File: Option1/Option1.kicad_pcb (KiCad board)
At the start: 2 copper layers, 86 x 69.5 mm, 115 parts, among them J1501 GH-13AB, J1801 Conn_01x08_Socket, J401 Conn_01x05_Pin, J402 Conn_01x04_Pin, J403 Conn_01x05_Pin, J503 KF2EDGKRG-3.5-2*7P, Q1001 JY2302, Q1101 JY2302, Q1401 BC817-40, Q1402 BC817-40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

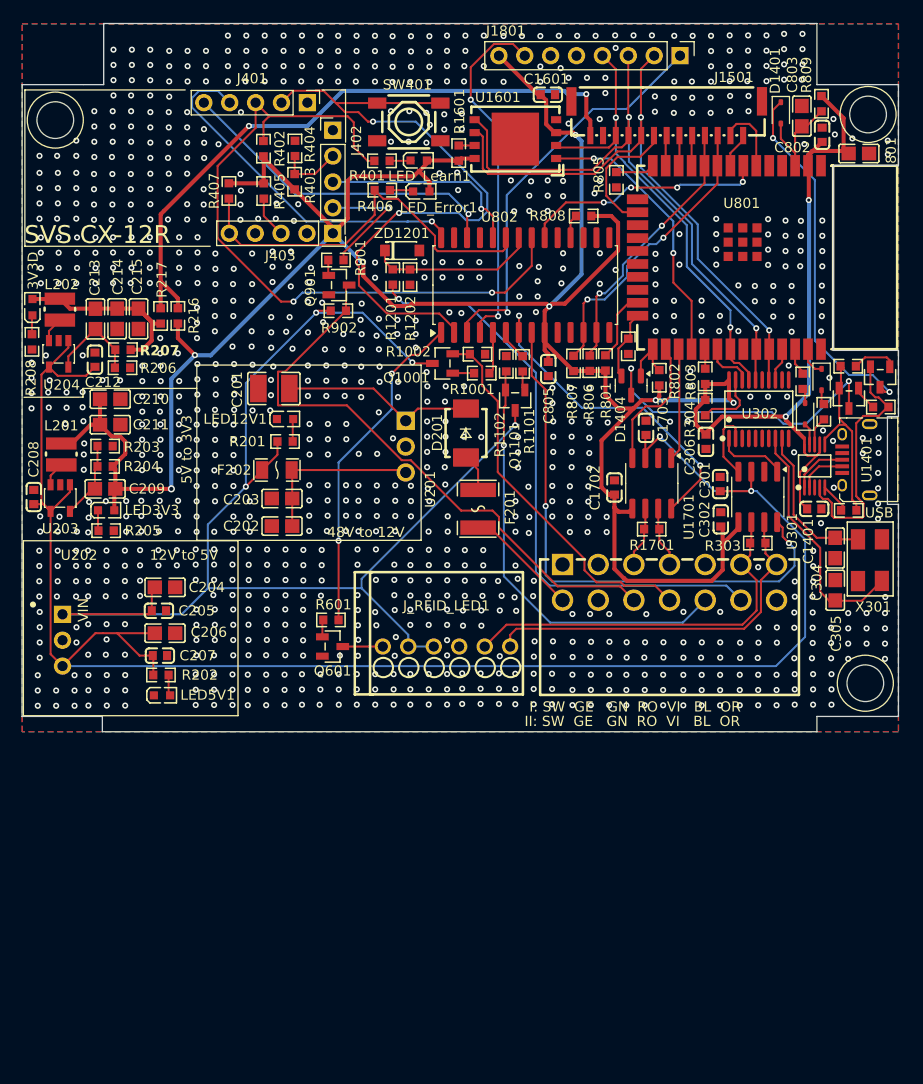
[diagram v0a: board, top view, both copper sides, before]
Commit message: Stecker nach hinten verschoben, Platine am vorderen Rand verlängert, Farbprints + Ref Feld hinzugefügt, Review eingearbeitet: Leiterbahnen dicker gemacht für Spannungsversorgung, Löcher verschoben, KeepOut Area vergrößert
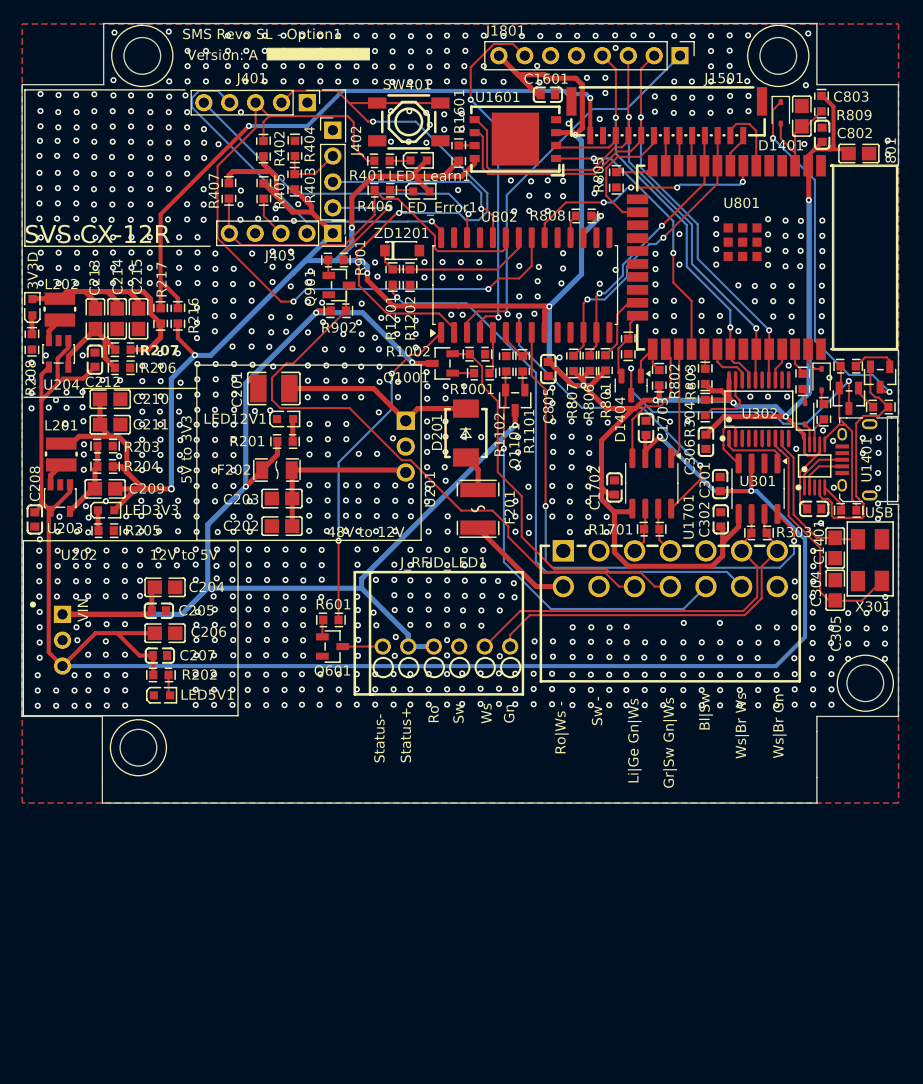
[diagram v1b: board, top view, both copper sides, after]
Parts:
- moved C208 2.20 mm to (101.2, 92.6), turned to -90 degrees
- moved J503 1.34 mm to (163.6, 97.5)
- moved R303 1.00 mm to (172.3, 94.0)
- moved U301 0.81 mm to (172.2, 89.6)
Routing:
- net 3.3V: track 310.7 -> 338.5 mm, vias 9 -> 12
- net /Powersupply/3.3V_D1: track 19.8 -> 27.3 mm
- net 5V: track 173.2 -> 177.2 mm
- net Lernmodus: track 67.5 -> 65.4 mm
- net /CAN2_Tranciever/CAN_S-Mode: track 54.7 -> 52.7 mm
- net /CAN1 Tranciever/CAN_H: track 6.51 -> 4.64 mm
- net Net-(U204-FB): track 9.45 -> 11.1 mm
- net /CAN1 Tranciever/CAN_L: track 5.95 -> 4.58 mm
- net /SOC Schalter/SOC_VCU: track 42.8 -> 41.5 mm
- net /RemoteDrive Schalter/RemoteDrive_VCU: track 36.9 -> 38.1 mm
- net /Stecker Input/VCU_LED: track 58.9 -> 57.8 mm
- net /CAN2_Tranciever/CAN_RX: track 7.00 -> 6.26 mm
- net GND: vias 1017 -> 991
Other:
- board size 86 x 69.5 mm -> 86 x 76.5 mm
- board text added: "Bl|Sw"
- board text added: "Gn"
- board text added: "Gr|Sw Gn|Ws"
- board text added: "Li|Ge Gn|Ws"
- board text added: "Ro"
- board text added: "Ro|Ws -"
- board text added: "SMS Revo SL - Option1"
- board text added: "Status+"
- board text added: "Status-"
- board text added: "Sw"
- board text added: "Sw -"
- board text added: "Version: A"
- board text added: "Ws"
- board text added: "Ws|Br Gn"
- board text added: "Ws|Br Ws"
- board text removed: "I: SW GE GN RO VI BL OR"
- board text removed: "II: SW GE GN RO VI BL OR"
- board text removed: "SMS Revo SL - Option1 - V1.0"

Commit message: Minimale Änderungen, Ausschnitt für USB Größer
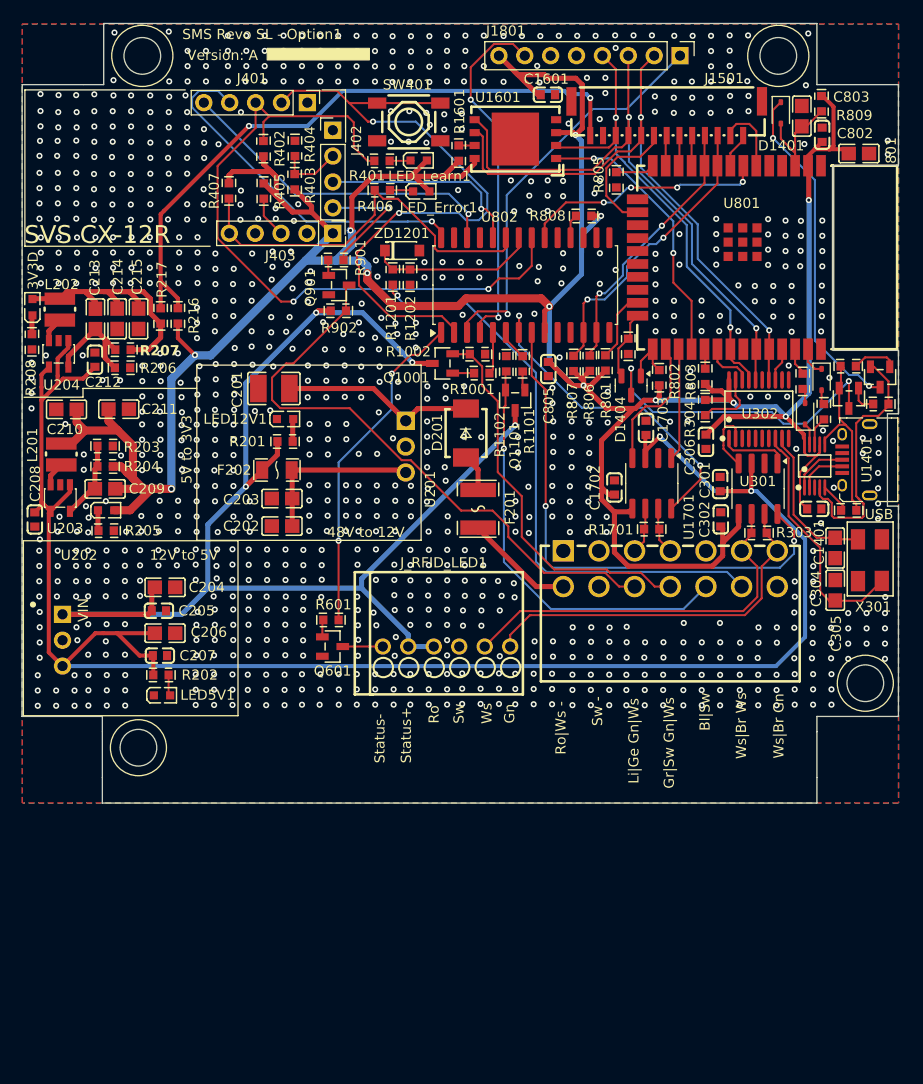
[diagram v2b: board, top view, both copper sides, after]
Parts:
- moved C210 4.41 mm to (104.3, 81.8), turned to 180 degrees
- moved C211 1.74 mm to (109.4, 81.8)
- moved R1404 0.30 mm to (184.2, 81.3)
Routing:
- net Net-(D1401-K): track 35.9 -> 33.8 mm
- net 3.3V: track 338.5 -> 339.8 mm
- net GND: vias 991 -> 973
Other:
- outline, holes or cut-outs redrawn

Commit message: LEDs für RX Ausgänge des Funkmodules hinzugefügt
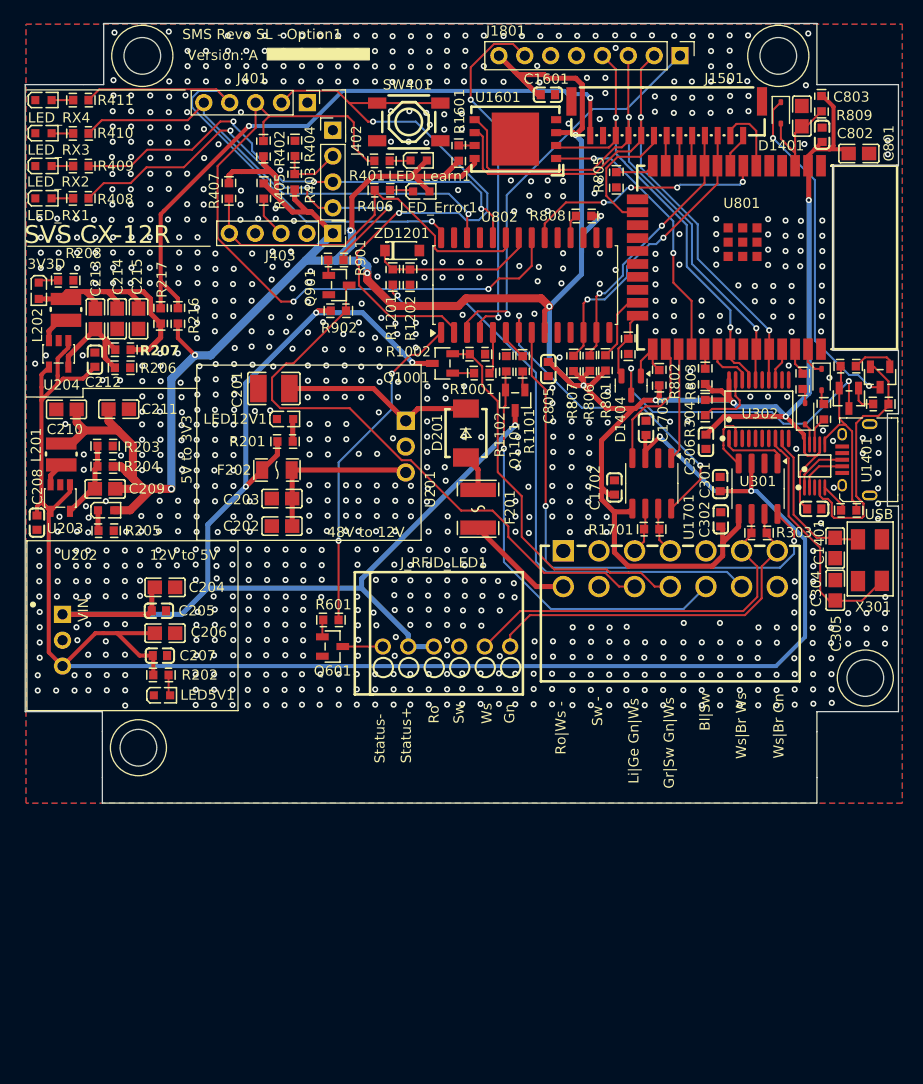
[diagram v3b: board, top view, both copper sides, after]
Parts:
- added LED_RX1: XL-1608SYGC-06, easyeda2kicad:LED0603-RD_GREEN, F.Cu at (102.0, 61.1)
- added LED_RX2: XL-1608SYGC-06, easyeda2kicad:LED0603-RD_GREEN, F.Cu at (102.0, 58.0)
- added LED_RX3: XL-1608SYGC-06, easyeda2kicad:LED0603-RD_GREEN, F.Cu at (102.0, 54.7)
- added LED_RX4: XL-1608SYGC-06, easyeda2kicad:LED0603-RD_GREEN, F.Cu at (102.0, 51.5)
- added R408: 220Ω, easyeda2kicad:R0603, F.Cu at (105.7, 61.1)
- added R409: 220Ω, easyeda2kicad:R0603, F.Cu at (105.7, 58.0)
- added R410: 220Ω, easyeda2kicad:R0603, F.Cu at (105.7, 54.8)
- added R411: 220Ω, easyeda2kicad:R0603, F.Cu at (105.7, 51.5)
- moved R208 6.89 mm to (104.2, 69.2), turned to 0 degrees
- moved 3V3D 1.72 mm to (101.6, 70.2), turned to -90 degrees
- moved L202 0.60 mm to (104.2, 72.0)
- moved C208 0.37 mm to (101.4, 93.0)
- renumbered 801 to C801
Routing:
- net RX_1: track 12.3 -> 42.9 mm, vias 1 -> 3
- net RX_2: track 19.9 -> 48.8 mm, vias 1 -> 3
- net RX_4: track 35.3 -> 50.2 mm
- net RX_3: track 32.7 -> 46.0 mm
- net Net-(LED_RX3-A): track 0.00 -> 2.13 mm
- net Net-(LED_RX4-A): track 0.00 -> 2.12 mm
- net Net-(LED_RX2-A): track 0.00 -> 2.12 mm
- net Net-(LED_RX1-A): track 0.00 -> 2.12 mm
- net /Powersupply/3.3V_D1: track 27.3 -> 26.7 mm
- net GND: vias 973 -> 925
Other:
- board size 86 x 76.5 mm -> 85.7 x 76.5 mm

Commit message: Kabelseitigen Stecker für JLC Bestellung hinzugefügt. Footprint erstellt und 3D Modell hinzugefügt, Footprint/3DModell von 6Pin Stecker und Fuse korrigiert
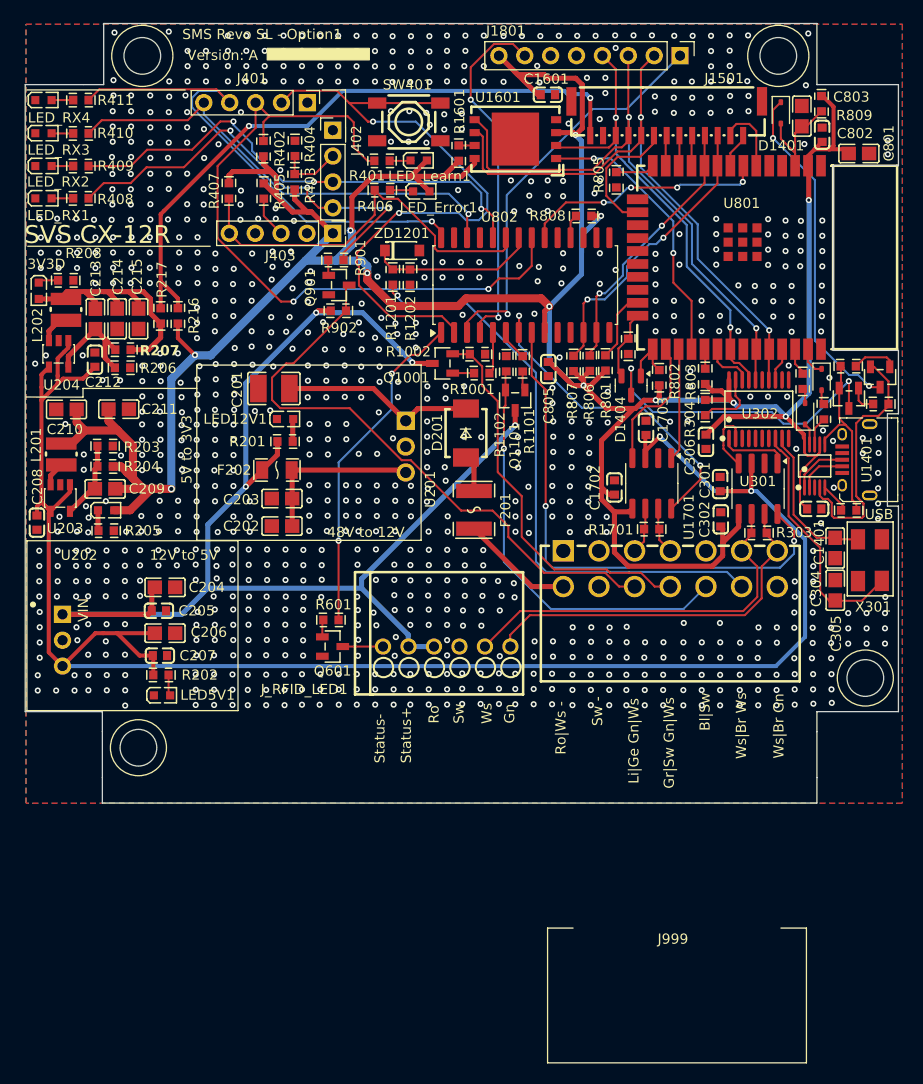
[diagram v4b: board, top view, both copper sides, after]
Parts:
- added J999: Phoenix_Connetor_07x2pin_toWire, easyeda2kicad:Phonix_Connector_07x2pin_toWire, F.Cu at (151.5, 146.0)
- moved J_RFID_LED1 10.1 mm to (132.6, 109.8)
- moved F201 3.31 mm to (146.3, 94.5)

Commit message: Platine verkleinert, um besser in gehäuse zu passen, PullUp Widerstand an Button hinzugefügt
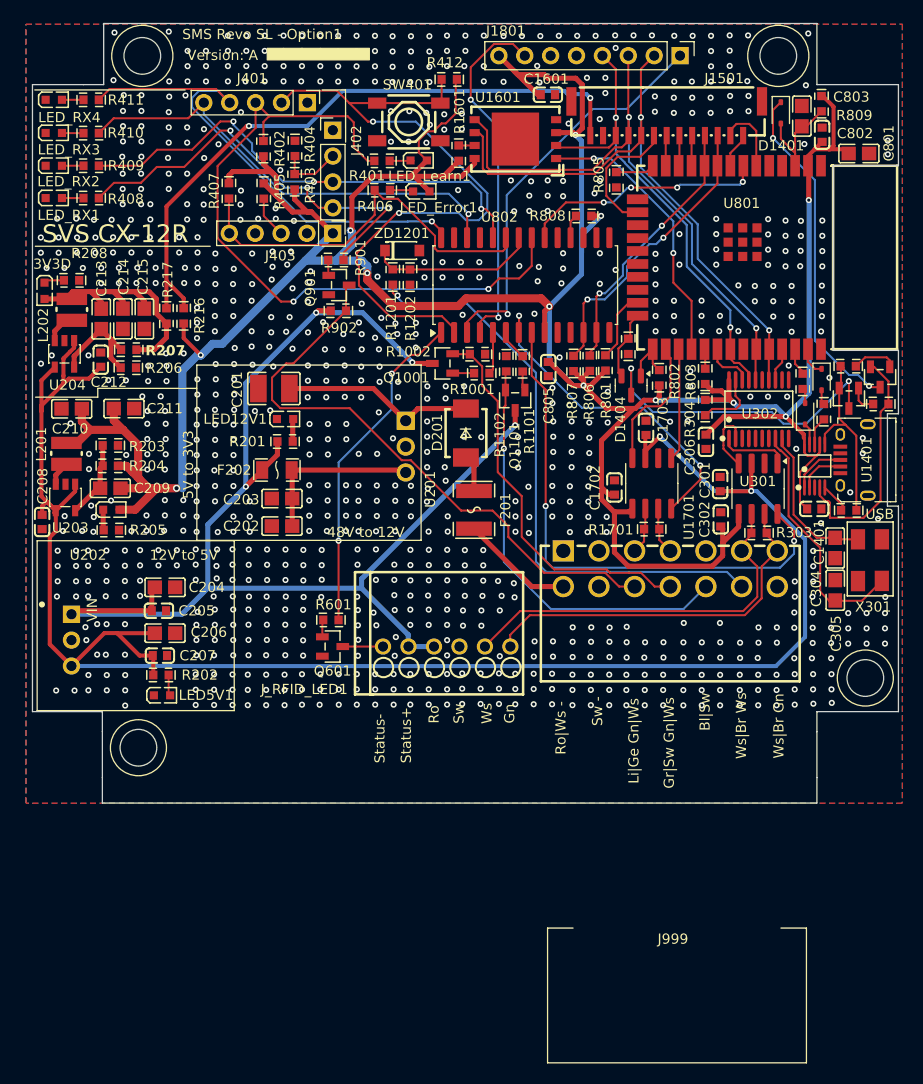
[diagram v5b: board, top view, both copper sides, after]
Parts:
- added R412: 10k, easyeda2kicad:R0603, F.Cu at (141.9, 49.5)
- moved R408 1.01 mm to (106.7, 61.1)
- moved R409 1.01 mm to (106.7, 57.9)
- moved R410 1.01 mm to (106.7, 54.7)
- moved R411 1.01 mm to (106.7, 51.5)
- moved LED_RX1 1.01 mm to (103.1, 61.1)
- moved LED_RX2 1.01 mm to (103.1, 57.9)
- moved LED_RX3 1.01 mm to (103.1, 54.7)
- moved LED_RX4 1.01 mm to (103.1, 51.5)
- moved U202 0.88 mm to (104.8, 104.5)
- moved C214 0.57 mm to (109.8, 73.0)
- moved R206 0.57 mm to (110.4, 77.8)
- moved R208 0.57 mm to (104.8, 69.2)
- moved 3V3D 0.57 mm to (102.1, 70.2)
- moved C212 0.57 mm to (107.7, 77.0)
- moved C213 0.57 mm to (107.7, 73.0)
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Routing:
- net 3.3V: track 340.1 -> 349.9 mm
- net Lernmodus: track 65.4 -> 67.8 mm
- net 12V: track 127.9 -> 126.1 mm
- net Net-(U1401-~{RTS}): track 25.0 -> 23.8 mm
- net RX_3: track 46.0 -> 44.9 mm
- net RX_2: track 48.8 -> 47.7 mm
- net RX_1: track 42.9 -> 41.9 mm
- net RX_4: track 50.2 -> 49.2 mm
- net 5V: track 177.4 -> 178.2 mm
- net GND: vias 925 -> 886
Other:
- board size 85.7 x 76.5 mm -> 85 x 76.5 mm

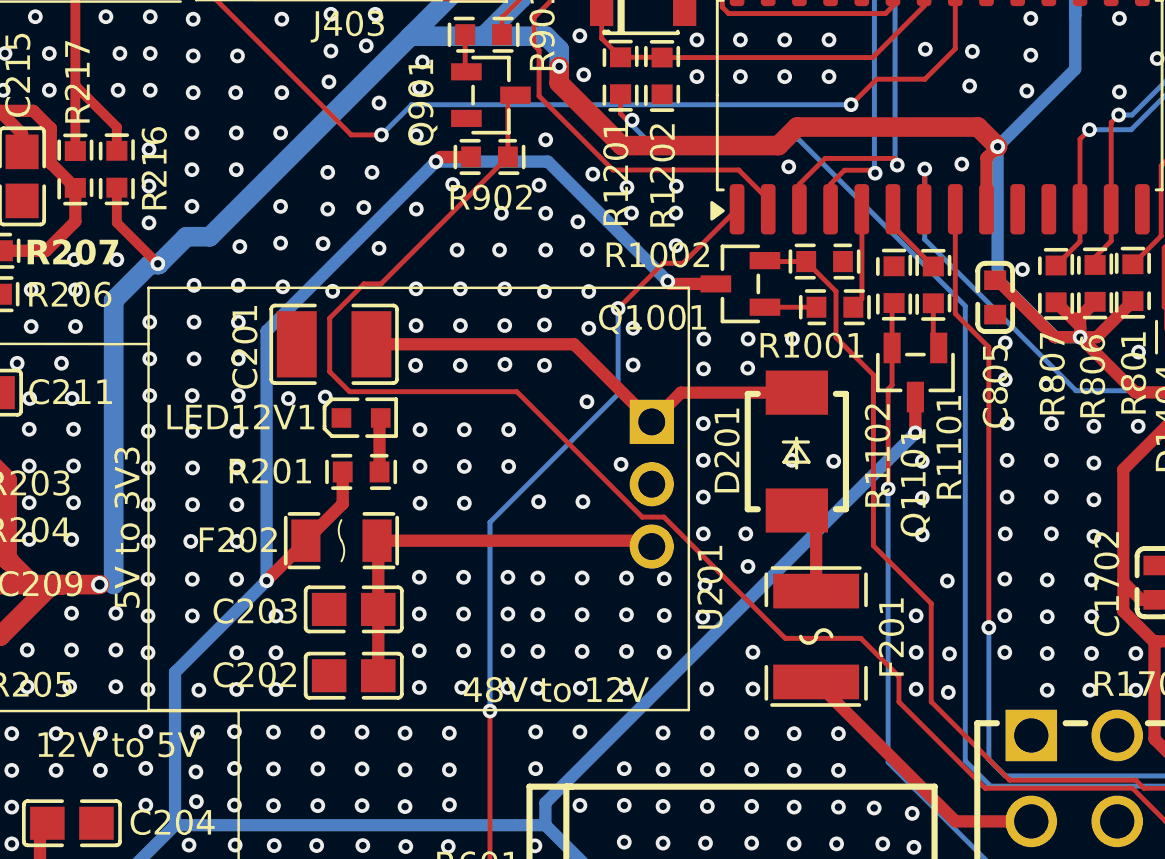
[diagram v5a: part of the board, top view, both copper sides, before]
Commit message: LEDs an Transistoren hinzugefügt, Layout angepasst, LEDs eingefügt, LEDs zeigen an, ob Transsitor durchgeschalten ist
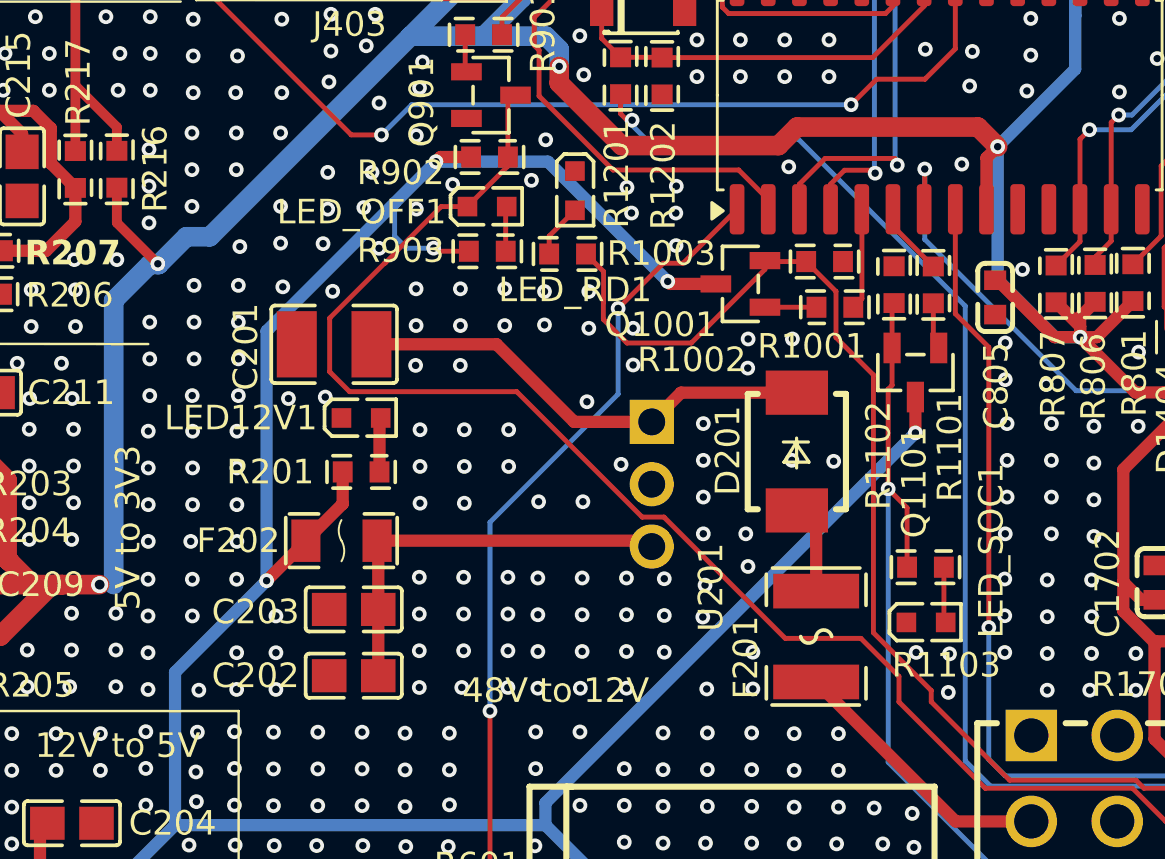
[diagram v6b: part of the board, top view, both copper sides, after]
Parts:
- added LED_OFF1: XL-1608SYGC-06, easyeda2kicad:LED0603-RD_GREEN, F.Cu at (130.9, 74.2)
- added LED_RD1: XL-1608SYGC-06, easyeda2kicad:LED0603-RD_GREEN, F.Cu at (134.5, 73.5)
- added LED_SOC1: XL-1608SYGC-06, easyeda2kicad:LED0603-RD_GREEN, F.Cu at (148.8, 91.1)
- added R1003: 1.8kΩ, easyeda2kicad:R0603, F.Cu at (134.2, 76.1)
- added R1103: 1.8kΩ, easyeda2kicad:R0603, F.Cu at (148.7, 88.9)
- added R903: 1.8kΩ, easyeda2kicad:R0603, F.Cu at (130.9, 76.0)
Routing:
- net /RemoteDrive Schalter/RemoteDrive_VCU: track 38.1 -> 49.7 mm
- net 12V: track 126.1 -> 130.7 mm, vias 4 -> 5
- net /SOC Schalter/SOC_VCU: track 41.5 -> 45.0 mm
- net Net-(LED_SOC1-A): track 0.00 -> 2.46 mm
- net Net-(LED_RD1-A): track 0.00 -> 2.21 mm
- net Net-(LED_OFF1-A): track 0.00 -> 1.84 mm
- net GND: vias 886 -> 868
